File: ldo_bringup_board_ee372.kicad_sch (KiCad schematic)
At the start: 75 parts, among them J1 VIN, J10 MD_SW_EN, J13 VSIG, J14 VSIG_BUF, J2 GND, J3 IBIAS, J4 VOUT, J5 VIN_SMA, J6 VOUT_SMA, J7 GND, J8 5V, Q1 FDV305N, Q2 FDV305N, Q3 FDV305N, Q4 FDV305N, Q5 FDV305N, SW1 SW_SPDT, U1 LDO_DualMode_BGR_EE372

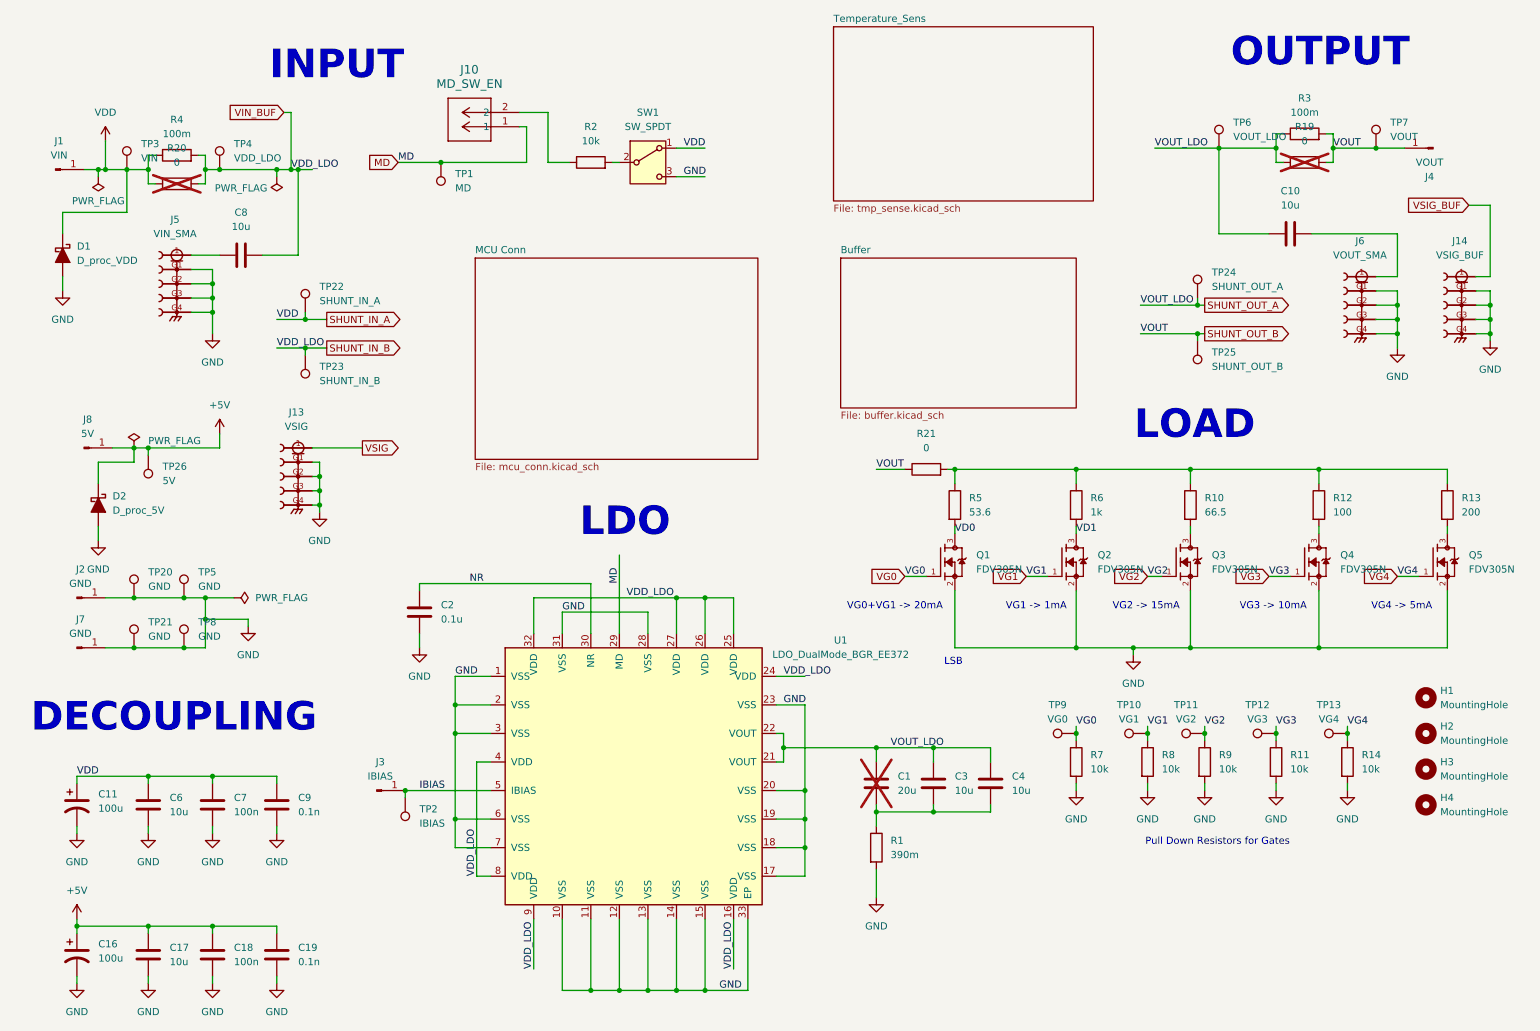
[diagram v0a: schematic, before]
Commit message: Add noise amplifier sheet, fill part fields, consolidate 10u and 100n caps
Noise amplifier: OPA4388 with three x11 stages, outputs at x121 and x1331
on J16 and J17, enabled by J15. Footprints and part fields on all its parts.
C2 moves to the same 0805 100n as the other 0.1u caps. Every 10u except the
C3 and C4 compensation pair moves to the 10% Murata GRM319R61E106KA12D.

Co-Authored-By: Claude Opus 5.5 (1M context) <noreply@anthropic.com>
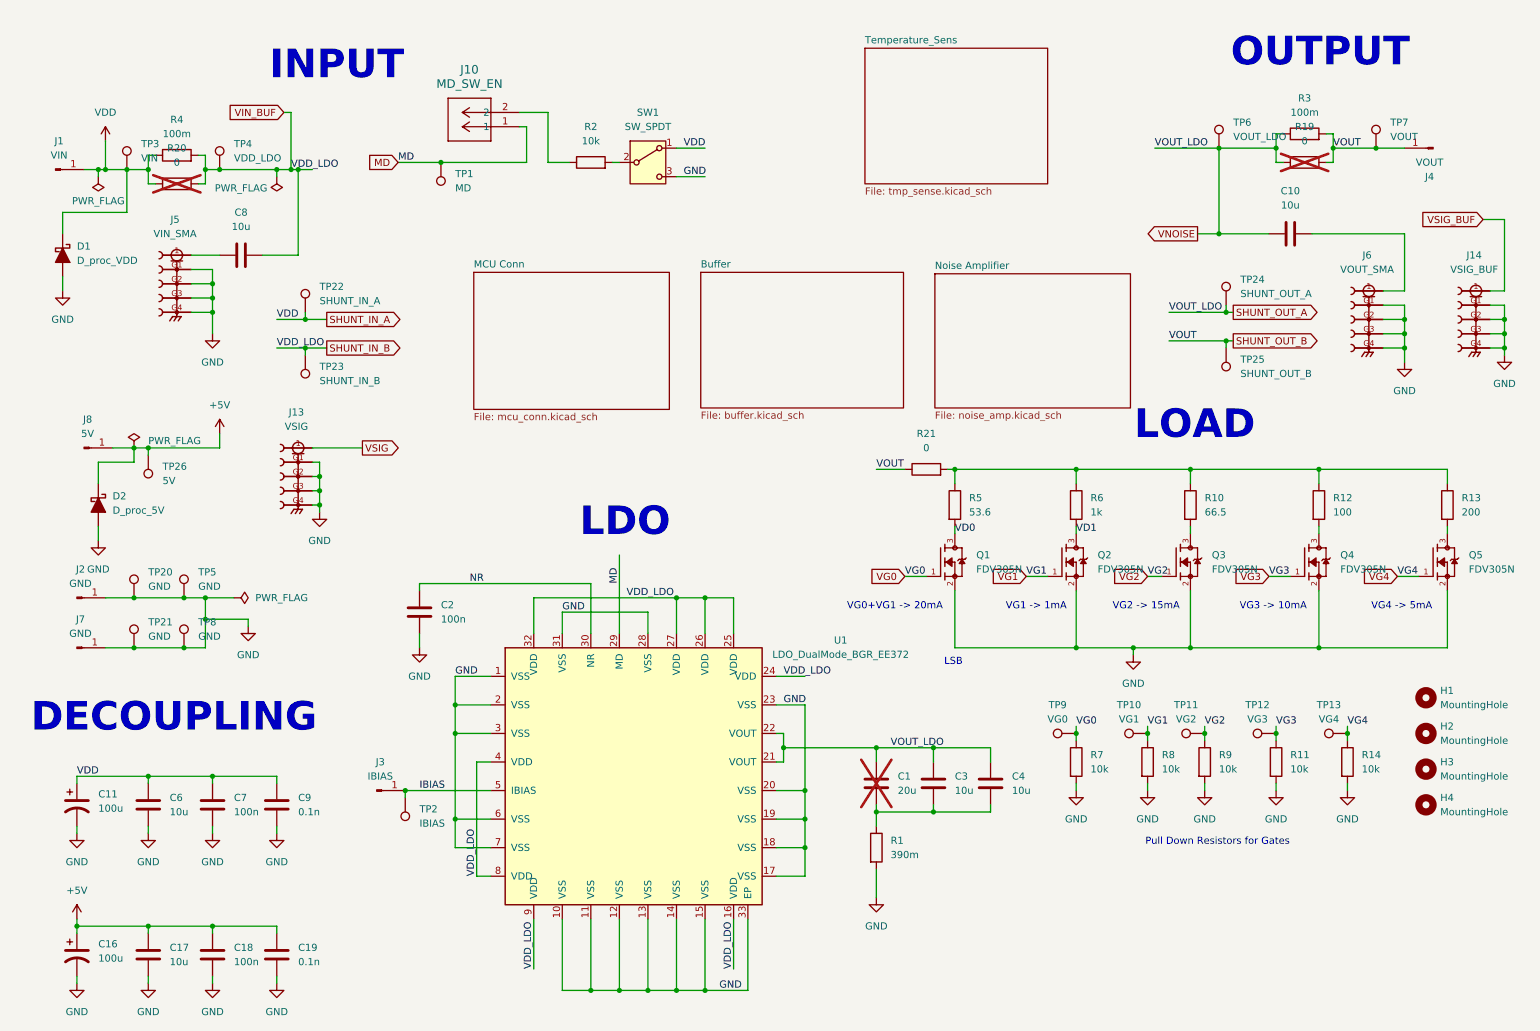
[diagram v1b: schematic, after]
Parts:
- C10, C17, C6, C8: Distributer Link 1 https://www.digikey.com/en/products/detail/kemet/C1206C106J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 -> https://www.digikey.com/en/products/detail/murata-electroni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; Manufacturer KEMET -> Murata Electronics; Manufacturer Part Number C1206C106J3RACAUTO -> GRM319R61E106KA12D
- C2: value 0.1u -> 100n; footprint Capacitor_SMD:C_0603_1608Metric_Pad1.08x0.95mm_HandSolder -> Capacitor_SMD:C_0805_2012Metric_Pad1.18x1.45mm_HandSolder; Distributer Link 1 https://www.digikey.com/en/products/detail/murata-electroni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 -> https://www.digikey.com/en/products/detail/samsung-electro-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; Manufacturer Murata Electronics -> Samsung Electro-Mechanics; Manufacturer Part Number GRM188R72A104KA35D -> CL21B104KBCNNNC
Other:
- added sheet Noise Amplifier (noise_amp.kicad_sch)
- moved on the sheet: J14, J6, TP24, TP25
